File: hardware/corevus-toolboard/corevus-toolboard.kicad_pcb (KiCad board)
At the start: 4 copper layers, 49.8 x 25.6 mm, 78 parts, among them J1 MF3, J10 1x3P, J2 XH, J3 MF3, J4 XH, J5 XH, J6 XH, J7 XH, J8 pinheader, J9 XH, Q2 NMOS, Q3 AO3401A, Q4 AO3400, Q5 AO3400, SW1 RST, U1 LIS2DE12, U2 TPS54302, U3 STM32G431KBU3, U4 TMC2209-LA, U5 MCP1416, U6 SPX3819M5-L-3-3, Y1 XRCGB25

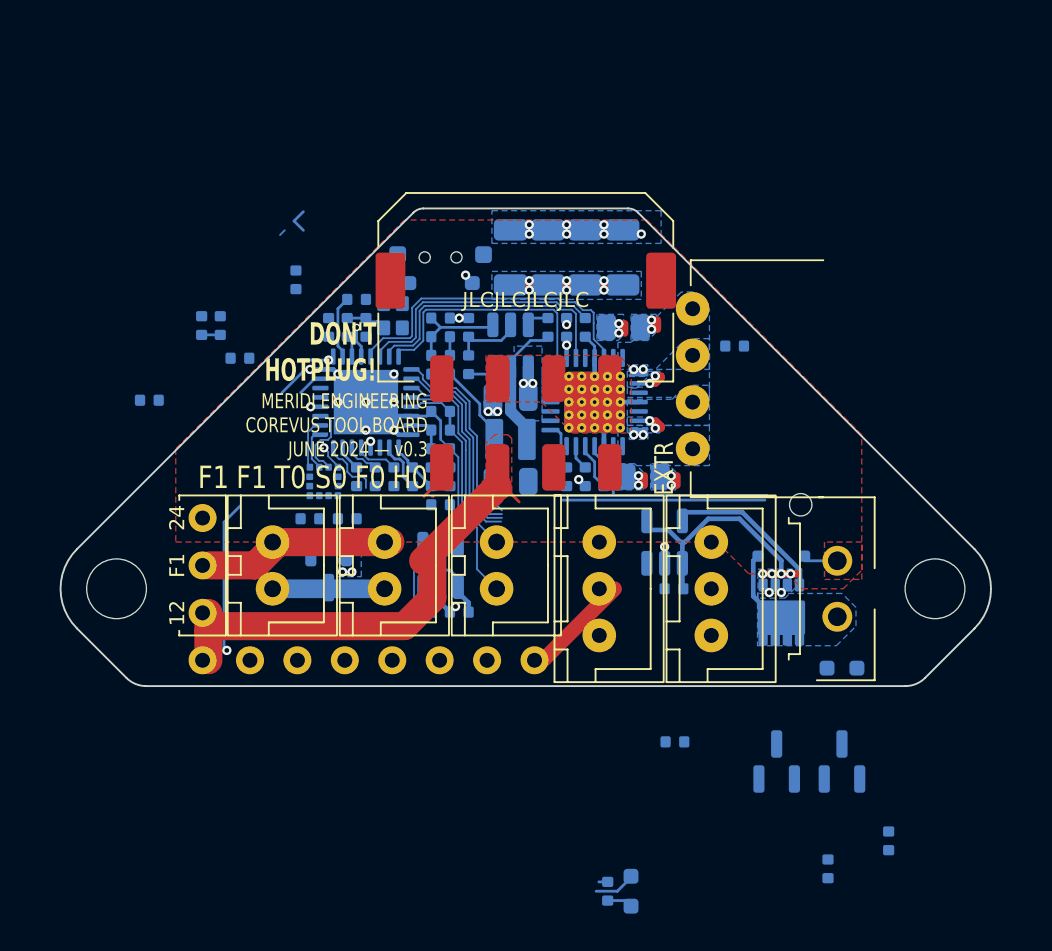
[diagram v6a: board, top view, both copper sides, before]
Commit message: added ctb v0.3 and dual 2160, fixed typo in v0.6 manual
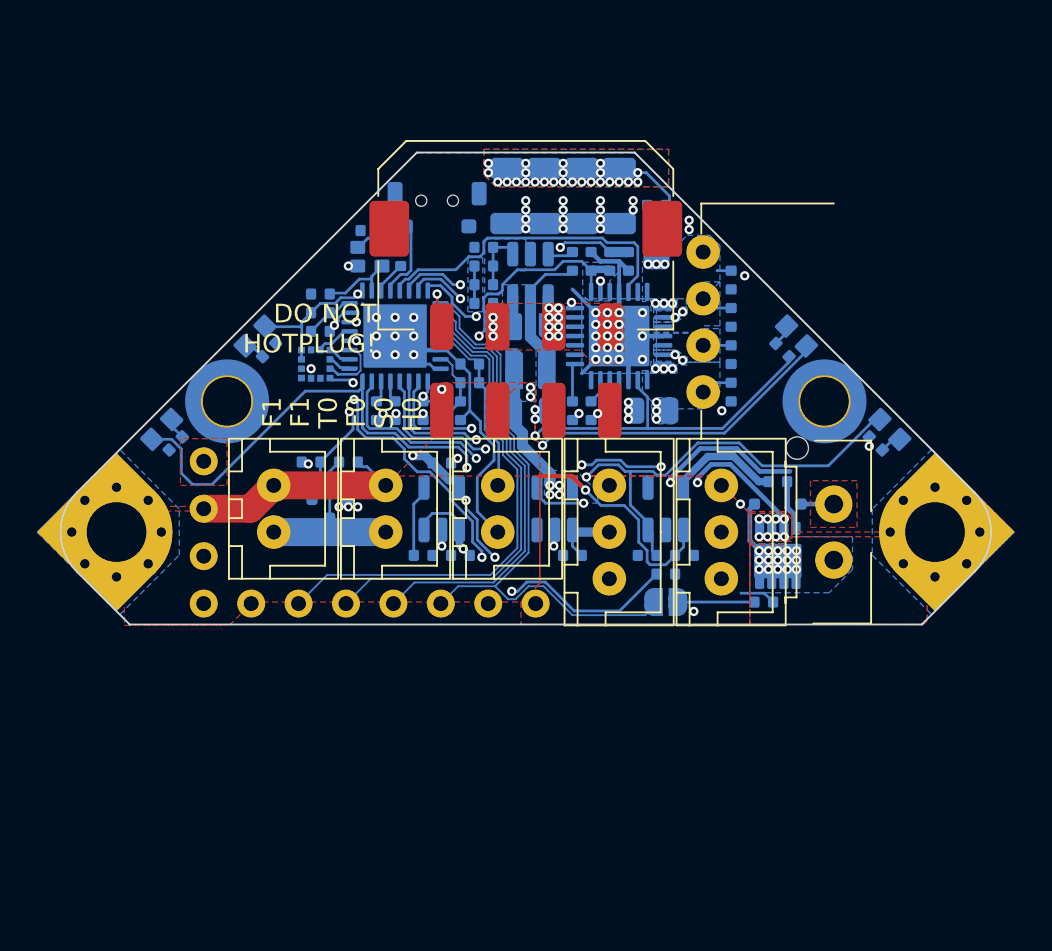
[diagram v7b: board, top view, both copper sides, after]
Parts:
- removed C10: 100nF, AlphaLib:0402C
- removed C27: 1µF, AlphaLib:0402C
- removed Q3: AO3401A, Package_TO_SOT_SMD:SOT-23
- removed Q5: AO3400, Package_TO_SOT_SMD:SOT-23
- removed R18: 10kΩ, AlphaLib:0402R
- removed U5: MCP1416, Package_TO_SOT_SMD:SOT-23-5
- added C18: 470pF, AlphaLib:0402C, B.Cu at (11.0, -13.5)
- added C19: 470pF, AlphaLib:0402C, B.Cu at (11.0, -11.5)
- added C20: 470pF, AlphaLib:0402C, B.Cu at (11.0, -9.50)
- added C21: 470pF, AlphaLib:0402C, B.Cu at (11.0, -7.50)
- added C6: 1µF, AlphaLib:0402C, B.Cu at (2.50, 1.25)
- added D5: Red, PCM_ME_passives:0603LED, B.Cu at (-19.5, -5.50)
- added H3: M2 Standoff, corevus:Sinhoo_TH162010, B.Cu at (-16.0, -7.00)
- added H4: M2 Standoff, corevus:Sinhoo_TH162010, B.Cu at (16.0, -7.00)
- added JP1: Jumper_2_Small_Open, Jumper:SolderJumper-2_P1.3mm_Open_RoundedPad1.0x1.5mm, B.Cu at (7.50, 3.75)
- added TH2: 10kΩ 3950K, AlphaLib:0402R, B.Cu at (12.8, 3.75)
- added U7: TPS2069CDBV, Package_TO_SOT_SMD:SOT-23-5, B.Cu at (1.55, -1.25)
- added U8: UCC27517, Package_TO_SOT_SMD:SOT-23-5, B.Cu at (7.50, -1.25)
- C1, C34: value 2.2µF -> 1µF
- D2: value Red -> Ylw; footprint corevus:XL1606 -> PCM_ME_passives:0603LED
- D3: value Grn -> Blu; footprint corevus:XL1606 -> PCM_ME_passives:0603LED
- D4: footprint AlphaLib:0402LED -> PCM_ME_passives:0603LED
- H1, H2: value MountingHole -> M3 Hole; footprint MountingHole:MountingHole_3.2mm_M3 -> corevus:MountingHole_M3_Driver_Corner
- R2: value 10kΩ -> 100kΩ
- R7: value 2.2kΩ -> 4.7kΩ
- R8: value 510kΩ -> 2.2kΩ
- R9: value 100kΩ -> 0Ω
- moved D3 31.0 mm to (14.5, -10.5), turned to -45 degrees
- moved R21 30.5 mm to (13.8, -9.75), turned to 135 degrees
- moved R1 19.3 mm to (18.8, -4.75), turned to -45 degrees
- moved R9 18.5 mm to (13.5, -2.70), turned to 180 degrees
- moved R7 18.0 mm to (7.50, 2.25), turned to 180 degrees
- moved R16 16.8 mm to (4.50, -14.5)
- moved R8 16.2 mm to (-18.8, -4.75), turned to 45 degrees
- moved R19 16.1 mm to (6.50, 1.25), turned to 0 degrees
- moved D2 13.0 mm to (19.5, -5.50), turned to 135 degrees
- moved R2 9.88 mm to (-11.0, -10.8)
- moved R20 8.62 mm to (7.00, -17.5)
- moved J9 7.21 mm to (10.5, 0.00)
- moved C14 7.01 mm to (-1.00, -18.0)
- moved C17 6.68 mm to (5.00, -18.0)
- moved U1 6.30 mm to (-11.2, -9.00), turned to 180 degrees
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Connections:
- FB1 pad 1: +3.3V -> VDDA
- FB1 pad 2: VDDA -> +3.3V
- J8 pad 2: /PA4 -> GND
- J8 pad 3: /PA5 -> /PA7
- J8 pad 5: /PA7 -> /PA5
- J8 pad 6: GND -> /PA4
- Q2 pad 4: /H0_Gate -> Net-(Q2-G)
- R7 pad 1: Net-(Q3-G) -> /_{FET}Therm
- R7 pad 2: +5V -> +3.3V
- R8 pad 1: +12V -> GND
- R8 pad 2: Net-(U2-EN) -> Net-(D5-K)
- R9 pad 1: Net-(U2-EN) -> Net-(Q2-G)
- R9 pad 2: GND -> /H0_Gate
- U1 pad 12: unconnected-(U1-INT1-Pad12) -> /ACCEL_INT1
- U2 pad 5: Net-(U2-EN) -> unconnected-(U2-EN-Pad5)
- U3 pad 19: /F0 -> /F0_FG
- U3 pad 20: /INT1 -> /S0
- U3 pad 24: /F1 -> /F0
- U3 pad 29: /F0_FG -> /ACCEL_INT1
- U3 pad 30: /S0 -> /F1
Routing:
- net +3.3V: track 19.5 -> 86.1 mm, vias 2 -> 8
- net /H0: track 1.37 -> 38.9 mm, vias 0 -> 2
- net /F0: track 0.31 -> 35.2 mm, vias 0 -> 2
- net +12V: track 38.6 -> 14.2 mm, vias 4 -> 3
- net /PA4: track 9.11 -> 31.9 mm
- net /S0: track 0.25 -> 21.1 mm, vias 0 -> 3
- net /PA7: track 10.1 -> 26.9 mm
- net /PA6: track 10.3 -> 25.2 mm
- net /F0_FG: track 0.31 -> 15.1 mm, vias 0 -> 1
- net /PA5: track 10.4 -> 23.5 mm
- net /~{En}: track 17.2 -> 28.0 mm, vias 0 -> 2
- net /D-: track 0.00 -> 9.95 mm, vias 0 -> 2
- net /F1: track 3.78 -> 12.4 mm, vias 0 -> 2
- net /_{FET}Therm: track 0.00 -> 5.66 mm
- net /BOOT0: track 16.2 -> 21.2 mm, vias 0 -> 3
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- added copper zone on B.Cu, net +12V
- added copper zone on In1.Cu, net +24V
- added copper zone on In2.Cu, net +24V
- added copper zone on B.Cu, net +3.3V
- added copper zone on B.Cu, net +5V
- added copper zone on F.Cu, net +5V
- added copper zone on B.Cu, net Net-(C28-Pad1)
- added copper zone on F.Cu, net Net-(D1-A)
- added copper zone on In1.Cu, net Net-(D1-A)
- added copper zone on In2.Cu, net Net-(D1-A)
- added copper zone on B.Cu, net Net-(U2-FB)
- added copper zone on In2.Cu, net Net-(U4-BRA)
- added copper zone on In2.Cu, net Net-(U4-BRB)
- removed copper zone on In1.Cu, net Net-(U4-BRA)
- removed copper zone on In1.Cu, net Net-(U4-BRB)
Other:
- board size 49.8 x 25.6 mm -> 49.8 x 25.3 mm
- board text added: "12V"
- board text added: "5V"
- board text added: "A4"
- board text added: "A5"
- board text added: "A6"
- board text added: "A7"
- board text added: "B8"
- board text added: "DO NOT HOTPLUG!"
- board text added: "GND"
- board text added: "HEAT"
- board text added: "HOT!"
- board text added: "MERIDI ENGINEERING JULY 2024 COREVUS TOOLBOARD v0.3"
- board text added: "PCF"
- board text added: "PWR"
- board text removed: "DON'T HOTPLUG!"
- board text removed: "JLCJLCJLCJLC"
- board text removed: "MERIDI ENGINEERING COREVUS TOOL BOARD JUNE 2024 — v0.3"

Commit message: last before i go on v0.7
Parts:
- C29: value 1µF 25V -> 100nF 25V
- D2: value Ylw -> Red
- D3: value Blu -> Grn
- D4: value Grn -> Wht
- D5: value Red -> Ylw
- moved R8 8.14 mm to (-11.0, -7.25), turned to 0 degrees
- moved R21 5.67 mm to (9.50, -6.00), turned to 0 degrees
- moved R1 4.70 mm to (14.5, -2.75), turned to 180 degrees
- moved R17 1.95 mm to (-12.5, -11.2), turned to 90 degrees
- moved R9 1.00 mm to (12.5, -2.75)
- moved D3 0.07 mm to (14.6, -10.6)
- moved D4 0.07 mm to (-14.6, -10.6)
- moved D2 0.07 mm to (19.6, -5.55)
- moved D5 0.07 mm to (-19.6, -5.55), turned to 45 degrees
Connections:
- D2 pad 1: Net-(D2-K) -> GND
- D2 pad 2: /H0 -> Net-(D2-A)
- D4 pad 1: Net-(D4-K) -> GND
- D4 pad 2: +3.3V -> Net-(D4-A)
- D5 pad 1: Net-(D5-K) -> GND
- D5 pad 2: /F0 -> Net-(D5-A)
- J8 pad 8: +5V -> +3.3V
- R1 pad 1: GND -> Net-(D2-A)
- R1 pad 2: Net-(D2-K) -> /H0
- R17 pad 1: GND -> Net-(D4-A)
- R17 pad 2: Net-(D4-K) -> +3.3V
- R8 pad 1: GND -> Net-(D5-A)
- R8 pad 2: Net-(D5-K) -> /F0
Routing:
- net +5V: track 20.9 -> 34.1 mm, vias 5 -> 4
- net /F0: track 35.2 -> 22.5 mm
- net Net-(D5-A): track 0.00 -> 9.46 mm
- net /~{En}: track 28.0 -> 21.4 mm
- net Net-(D2-A): track 0.00 -> 6.12 mm
- net Net-(D3-K): track 1.16 -> 7.28 mm
- net /H0: track 38.9 -> 34.2 mm
- net /BOOT0: track 21.2 -> 23.7 mm
- net Net-(D4-A): track 0.00 -> 1.73 mm
- net Net-(D2-K): track 1.16 -> 0.00 mm
- net Net-(D5-K): track 1.16 -> 0.00 mm
- net Net-(D4-K): track 1.16 -> 0.00 mm
- net /H0_Gate: track 6.01 -> 5.11 mm
- net GND: track 39.1 -> 38.7 mm, vias 85 -> 83
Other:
- board size 49.8 x 25.3 mm -> 49.8 x 25.5 mm
- board text added: "3V3"
- board text added: "RESET"
- board text added: "TOOLBOARD v0.3"
- board text added: "corevus"
- board text removed: "5V"
- board text removed: "RST"
